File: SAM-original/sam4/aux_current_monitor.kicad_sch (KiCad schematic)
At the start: 8 parts, among them U6 LM3480-3.3, U7 ACS71240LLCBTR-030B3

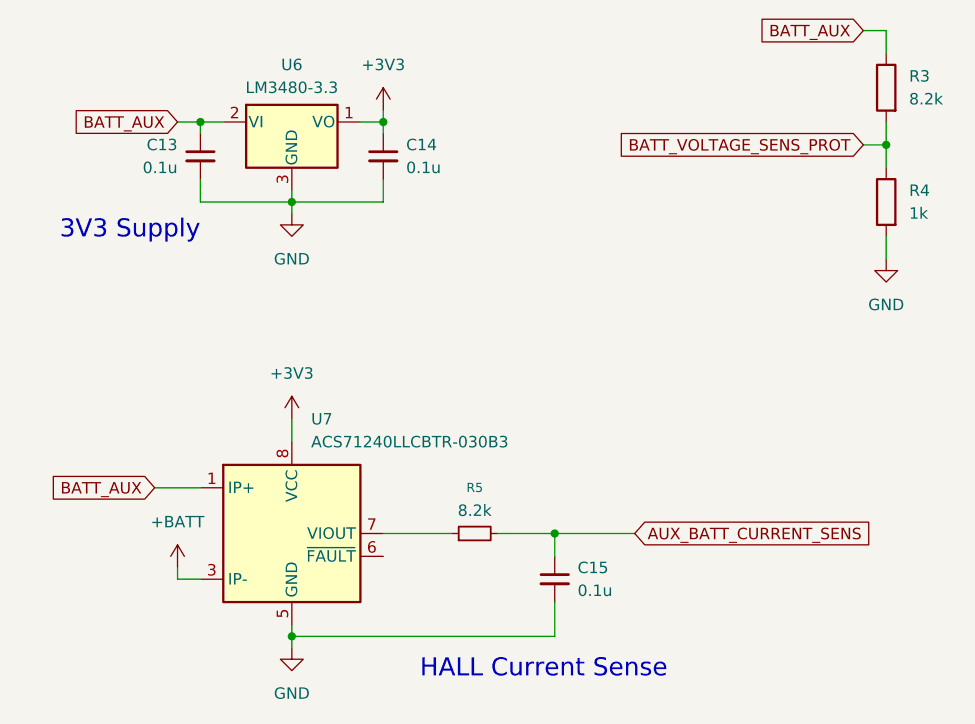
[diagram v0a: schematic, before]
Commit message: reannotate sam schem to bring into parity
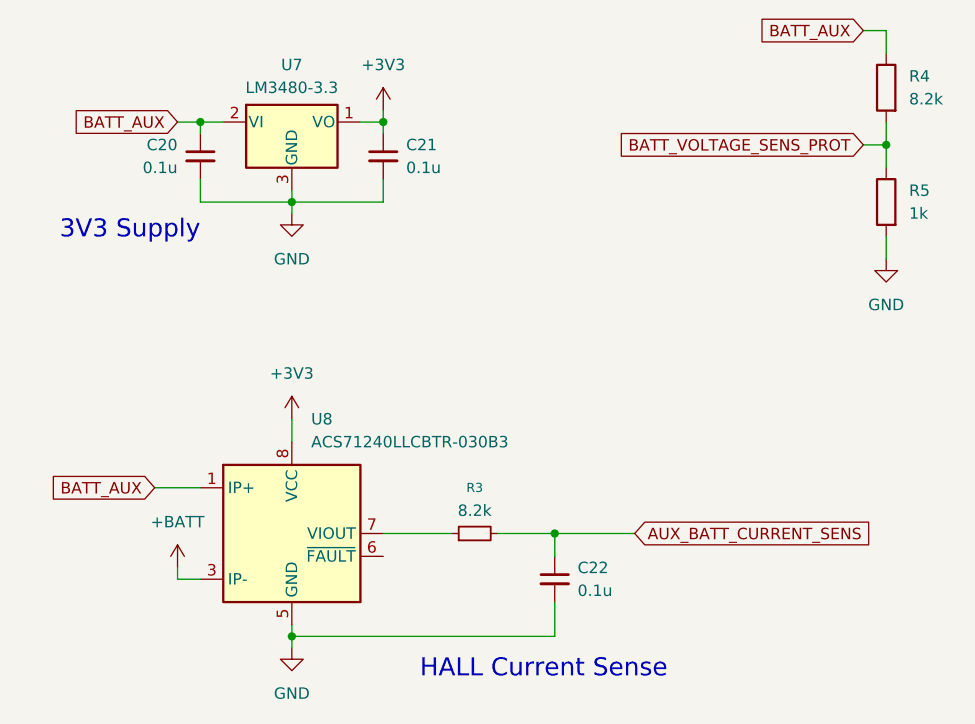
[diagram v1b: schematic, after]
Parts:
- renumbered C13 to C20, C14 to C21, C15 to C22, R5 to R3, R3 to R4, R4 to R5, U6 to U7, U7 to U8
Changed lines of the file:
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@@
 		(dnp no)
 		(fields_autoplaced yes)
-		(property "Reference" "U7"
+		(property "Reference" "U8"
 			(at 49.1333 67.31 0)
 			(effects
@@
 			(project ""
 				(path "/01aa8038-f16d-42dc-9377-7a3d64116781/b5606cfd-548c-4698-9c0c-2e0d315776b1"
-					(reference "U7")
+					(reference "U8")
 					(unit 1)
 				)
@@
 		(on_board yes)
 		(dnp no)
-		(property "Reference" "C14"
+		(property "Reference" "C21"
 			(at 59.69 36.8362 0)
 			(effects
@@
 			(project "sam4"
 				(path "/01aa8038-f16d-42dc-9377-7a3d64116781/b5606cfd-548c-4698-9c0c-2e0d315776b1"
-					(reference "C14")
+					(reference "C21")
 					(unit 1)
 				)
@@
 		(dnp no)
 		(fields_autoplaced yes)
-		(property "Reference" "R4"
+		(property "Reference" "R5"
 			(at 115.57 41.9099 0)
 			(effects
@@
 			(project "sam4"
 				(path "/01aa8038-f16d-42dc-9377-7a3d64116781/b5606cfd-548c-4698-9c0c-2e0d315776b1"
-					(reference "R4")
+					(reference "R5")
 					(unit 1)
 				)
@@
 		(on_board yes)
 		(dnp no)
-		(property "Reference" "C13"
+		(property "Reference" "C20"
 			(at 34.29 36.8362 0)
 			(effects
@@
 			(project ""
 				(path "/01aa8038-f16d-42dc-9377-7a3d64116781/b5606cfd-548c-4698-9c0c-2e0d315776b1"
-					(reference "C13")
+					(reference "C20")
 					(unit 1)
 				)
@@
 		(dnp no)
 		(fields_autoplaced yes)
-		(property "Reference" "R5"
+		(property "Reference" "R3"
 			(at 67.31 74.93 90)
 			(effects
@@
 			(project ""
 				(path "/01aa8038-f16d-42dc-9377-7a3d64116781/b5606cfd-548c-4698-9c0c-2e0d315776b1"
-					(reference "R5")
+					(reference "R3")
 					(unit 1)
 				)
@@
 		(dnp no)
 		(fields_autoplaced yes)
-		(property "Reference" "U6"
+		(property "Reference" "U7"
 			(at 46.99 27.94 0)
 			(effects
@@
 			(project ""
 				(path "/01aa8038-f16d-42dc-9377-7a3d64116781/b5606cfd-548c-4698-9c0c-2e0d315776b1"
-					(reference "U6")
+					(reference "U7")
 					(unit 1)
 				)
@@
 		(dnp no)
 		(fields_autoplaced yes)
-		(property "Reference" "C15"
+		(property "Reference" "C22"
 			(at 78.74 83.8262 0)
 			(effects
@@
 			(project ""
 				(path "/01aa8038-f16d-42dc-9377-7a3d64116781/b5606cfd-548c-4698-9c0c-2e0d315776b1"
-					(reference "C15")
+					(reference "C22")
 					(unit 1)
 				)
@@
 		(dnp no)
 		(fields_autoplaced yes)
-		(property "Reference" "R3"
+		(property "Reference" "R4"
 			(at 115.57 29.2099 0)
 			(effects
@@
 			(project ""
 				(path "/01aa8038-f16d-42dc-9377-7a3d64116781/b5606cfd-548c-4698-9c0c-2e0d315776b1"
-					(reference "R3")
-					(unit 1)
-				)
+					(reference "R4")
+					(unit 1)
+				)

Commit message: add updated SAM4 routing (DRC clean) + model
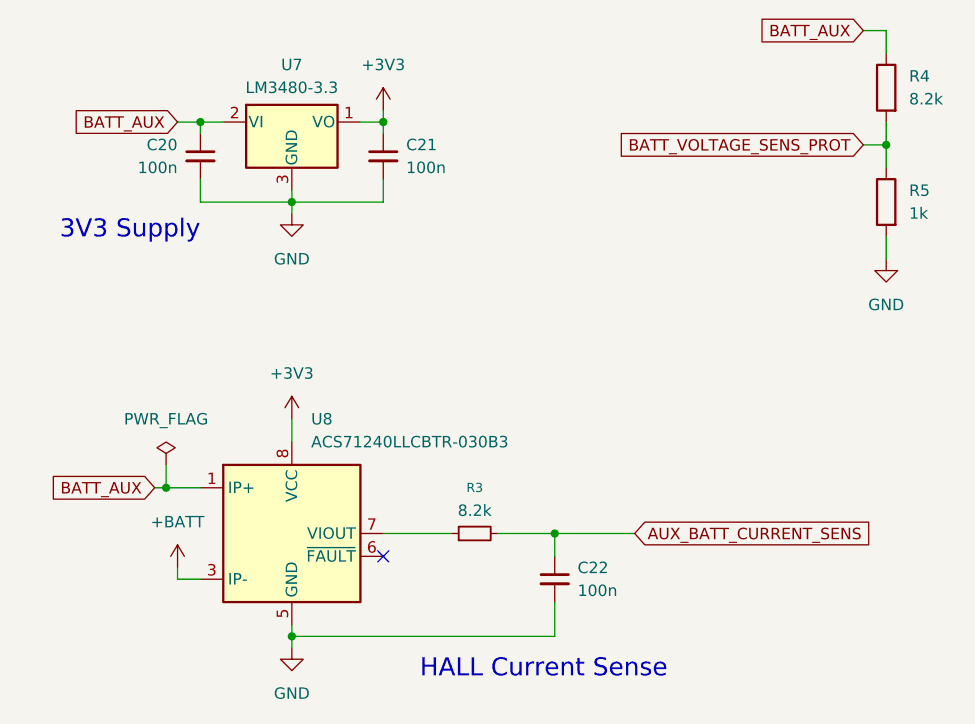
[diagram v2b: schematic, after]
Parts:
- C20, C21, C22: value 0.1u -> 100n; footprint Capacitor_SMD:C_1206_3216Metric_Pad1.33x1.80mm_HandSolder -> Capacitor_SMD:C_1206_3216Metric; LCSC (none) -> C24497
- R3, R4: footprint Resistor_SMD:R_1206_3216Metric_Pad1.30x1.75mm_HandSolder -> Resistor_SMD:R_0805_2012Metric_Pad1.20x1.40mm_HandSolder; LCSC (none) -> C17828
- R5: footprint Resistor_SMD:R_1206_3216Metric_Pad1.30x1.75mm_HandSolder -> Resistor_SMD:R_1206_3216Metric; LCSC (none) -> C4410
- U7: LCSC (none) -> C5380665
- U8: LCSC (none) -> C2654896
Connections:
- no-connect marks 0 -> 1
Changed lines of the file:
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@@
+	)
+	(junction
+		(at 33.02 74.93)
+		(diameter 0)
+		(color 0 0 0 0)
 	)
 	(junction
@@
 		(color 0 0 0 0)
 	)
+	(no_connect
+		(at 57.15 82.55)
+	)
 	(wire
 		(pts
@@
 	(wire
 		(pts
-			(xy 31.75 74.93) (xy 36.83 74.93)
+			(xy 33.02 74.93) (xy 36.83 74.93)
+		)
+		(stroke
+			(width 0)
+			(type default)
+		)
+	)
+	(wire
+		(pts
+			(xy 31.75 74.93) (xy 33.02 74.93)
+		)
+		(stroke
+			(width 0)
+			(type default)
+		)
+	)
+	(wire
+		(pts
+			(xy 33.02 72.39) (xy 33.02 74.93)
 		)
 		(stroke
@@
 		)
 		(property "Description" ""
+			(at 52.07 67.31 0)
+			(effects
+				(font
+					(size 1.27 1.27)
+				)
+				(hide yes)
+			)
+		)
+		(property "LCSC" "C2654896"
 			(at 52.07 67.31 0)
 			(effects
@@
 			)
 		)
-		(property "Value" "0.1u"
+		(property "Value" "100n"
 			(at 59.69 39.3762 0)
 			(effects
@@
 			)
 		)
-		(property "Footprint" "Capacitor_SMD:C_1206_3216Metric_Pad1.33x1.80mm_HandSolder"
+		(property "Footprint" "Capacitor_SMD:C_1206_3216Metric"
 			(at 57.15 38.1 0)
 			(effects
@@
 		)
 		(property "Description" "Unpolarized capacitor, small symbol"
+			(at 57.15 38.1 0)
+			(effects
+				(font
+					(size 1.27 1.27)
+				)
+				(hide yes)
+			)
+		)
+		(property "LCSC" "C24497"
 			(at 57.15 38.1 0)
 			(effects
@@
 			)
 		)
-		(property "Footprint" "Resistor_SMD:R_1206_3216Metric_Pad1.30x1.75mm_HandSolder"
+		(property "Footprint" "Resistor_SMD:R_1206_3216Metric"
 			(at 114.808 43.18 90)
 			(effects
@@
 		)
 		(property "Description" "Resistor"
+			(at 113.03 43.18 0)
+			(effects
+				(font
+					(size 1.27 1.27)
+				)
+				(hide yes)
+			)
+		)
+		(property "LCSC" "C4410"
 			(at 113.03 43.18 0)
 			(effects
@@
 			)
 		)
-		(property "Value" "0.1u"
+		(property "Value" "100n"
 			(at 34.29 39.3762 0)
 			(effects
@@
 			)
 		)
-		(property "Footprint" "Capacitor_SMD:C_1206_3216Metric_Pad1.33x1.80mm_HandSolder"
+		(property "Footprint" "Capacitor_SMD:C_1206_3216Metric"
 			(at 36.83 38.1 0)
 			(effects
@@
 		)
 		(property "Description" "Unpolarized capacitor, small symbol"
+			(at 36.83 38.1 0)
+			(effects
+				(font
+					(size 1.27 1.27)
+				)
+				(hide yes)
+			)
+		)
+		(property "LCSC" "C24497"
 			(at 36.83 38.1 0)
 			(effects
@@
 			)
 		)
-		(property "Footprint" "Resistor_SMD:R_1206_3216Metric_Pad1.30x1.75mm_HandSolder"
+		(property "Footprint" "Resistor_SMD:R_0805_2012Metric_Pad1.20x1.40mm_HandSolder"
 			(at 67.31 80.01 0)
 			(effects
@@
 		(property "Description" "Resistor, small symbol"
 			(at 67.31 80.01 0)
+			(effects
+				(font
+					(size 1.27 1.27)
+				)
+				(hide yes)
+			)
+		)
+		(property "LCSC" "C17828"
+			(at 67.31 80.01 90)
 			(effects
 				(font
@@
 			)
 		)
+		(property "LCSC" "C5380665"
+			(at 46.99 34.29 0)
+			(effects
+				(font
+					(size 1.27 1.27)
+				)
+				(hide yes)
+			)
+		)
 		(pin "3"
 		)
@@
 			)
 		)
-		(property "Value" "0.1u"
+		(property "Value" "100n"
 			(at 78.74 86.3662 0)
 			(effects
@@
 			)
 		)
-		(property "Footprint" "Capacitor_SMD:C_1206_3216Metric_Pad1.33x1.80mm_HandSolder"
+		(property "Footprint" "Capacitor_SMD:C_1206_3216Metric"
 			(at 76.2 85.09 0)
 			(effects
@@
 		)
 		(property "Description" "Unpolarized capacitor, small symbol"
+			(at 76.2 85.09 0)
+			(effects
+				(font
+					(size 1.27 1.27)
+				)
+				(hide yes)
+			)
+		)
+		(property "LCSC" "C24497"
 			(at 76.2 85.09 0)
 			(effects
@@
 				(path "/01aa8038-f16d-42dc-9377-7a3d64116781/b5606cfd-548c-4698-9c0c-2e0d315776b1"
 					(reference "#PWR019")
+					(unit 1)
+				)
+			)
+		)
+	)
+	(symbol
+		(lib_id "power:PWR_FLAG")
+		(at 33.02 72.39 0)
+		(unit 1)
+		(exclude_from_sim no)
+		(in_bom yes)
+		(on_board yes)
+		(dnp no)
+		(fields_autoplaced yes)
+		(property "Reference" "#FLG02"
+			(at 33.02 70.485 0)
+			(effects
+				(font
+					(size 1.27 1.27)
+				)
+				(hide yes)
+			)
+		)
+		(property "Value" "PWR_FLAG"
+			(at 33.02 67.31 0)
+			(effects
+				(font
+					(size 1.27 1.27)
+				)
+			)
+		)
+		(property "Footprint" ""
+			(at 33.02 72.39 0)
+			(effects
+				(font
+					(size 1.27 1.27)
+				)
+				(hide yes)
+			)
+		)
+		(property "Datasheet" "~"
+			(at 33.02 72.39 0)
+			(effects
+				(font
+					(size 1.27 1.27)
+				)
+				(hide yes)
+			)
+		)
+		(property "Description" "Special symbol for telling ERC where power comes from"
+			(at 33.02 72.39 0)
+			(effects
+				(font
+					(size 1.27 1.27)
+				)
+				(hide yes)
+			)
+		)
+		(pin "1"
+		)
+		(instances
+			(project ""
+				(path "/01aa8038-f16d-42dc-9377-7a3d64116781/b5606cfd-548c-4698-9c0c-2e0d315776b1"
+					(reference "#FLG02")
 					(unit 1)
 				)
@@
 			)
 		)
-		(property "Footprint" "Resistor_SMD:R_1206_3216Metric_Pad1.30x1.75mm_HandSolder"
+		(property "Footprint" "Resistor_SMD:R_0805_2012Metric_Pad1.20x1.40mm_HandSolder"
 			(at 114.808 30.48 90)
 			(effects
@@
 			(at 113.03 30.48 0)
 			(effects
+				(font
+					(size 1.27 1.27)
+				)
+				(hide yes)
+			)
+		)
+		(property "LCSC" "C17828"
+			(at 113.03 30.48 0)
+			(effects
